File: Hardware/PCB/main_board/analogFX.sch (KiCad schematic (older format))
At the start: 40 parts, among them Q1 BC547, U1 MCP6002-xSN, U4 RC4558

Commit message: Add FX buffer and headphone amp to schematics
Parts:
- added C33: 100n, Capacitor_SMD:C_0805_2012Metric, symbol Device:C
- added R20: 3.9k, Resistor_SMD:R_0805_2012Metric, symbol Device:R
- added R21: 10k, Resistor_SMD:R_0805_2012Metric, symbol Device:R
- Q1: value BC547 -> BC547B
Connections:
- net labels added: 2.5V_midpoint, IN_DIST, OUT_VCF
- net labels removed: OUT_VCF__IN_DIST
- wire segments 123 -> 127
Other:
- note added: "buffer"
- moved on the sheet: C1, R3, R5, R6, U1B
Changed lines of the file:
@@
-$EndComp
-$Comp
-L Amplifier_Operational:MCP6002-xSN U?
-U 2 1 5E64D29A
-P 6600 1950
-AR Path="/5E64D29A" Ref="U?"  Part="2"
-AR Path="/5E632F77/5E64D29A" Ref="U1"  Part="2"
-F 0 "U1" H 6600 2317 50  0000 C CNN
-F 1 "MCP6002-xSN" H 6600 2226 50  0000 C CNN
-F 2 "Package_SO:SOIC-8_3.9x4.9mm_P1.27mm" H 6600 1950 50  0001 C CNN
-F 3 "http://ww1.microchip.com/downloads/en/DeviceDoc/21733j.pdf" H 6600 1950 50  0001 C CNN
-	2    6600 1950
-	1    0    0    -1
 $EndComp
 $Comp
 L Device:R R?
 U 1 1 5E64D2A0
-P 3200 2800
+P 2850 2800
 AR Path="/5E64D2A0" Ref="R?"  Part="1"
 AR Path="/5E632F77/5E64D2A0" Ref="R6"  Part="1"
-F 0 "R6" H 3270 2846 50  0000 L CNN
-F 1 "100k" H 3270 2755 50  0000 L CNN
-F 2 "Resistor_SMD:R_0805_2012Metric" V 3130 2800 50  0001 C CNN
-F 3 "~" H 3200 2800 50  0001 C CNN
-	1    3200 2800
+F 0 "R6" H 2920 2846 50  0000 L CNN
+F 1 "100k" H 2920 2755 50  0000 L CNN
+F 2 "Resistor_SMD:R_0805_2012Metric" V 2780 2800 50  0001 C CNN
+F 3 "~" H 2850 2800 50  0001 C CNN
+	1    2850 2800
 	1    0    0    -1
 $EndComp
@@
 L power:+5VA #PWR?
 U 1 1 5E64D2A6
-P 2750 2550
+P 2400 2550
 AR Path="/5E64D2A6" Ref="#PWR?"  Part="1"
 AR Path="/5E632F77/5E64D2A6" Ref="#PWR04"  Part="1"
-F 0 "#PWR04" H 2750 2400 50  0001 C CNN
-F 1 "+5VA" V 2765 2677 50  0000 L CNN
-F 2 "" H 2750 2550 50  0001 C CNN
-F 3 "" H 2750 2550 50  0001 C CNN
-	1    2750 2550
+F 0 "#PWR04" H 2400 2400 50  0001 C CNN
+F 1 "+5VA" V 2415 2677 50  0000 L CNN
+F 2 "" H 2400 2550 50  0001 C CNN
+F 3 "" H 2400 2550 50  0001 C CNN
+	1    2400 2550
 	0    -1   -1   0
 $EndComp
@@
 L power:GND #PWR?
 U 1 1 5E64D2AC
-P 3200 3000
+P 2850 3000
 AR Path="/5E64D2AC" Ref="#PWR?"  Part="1"
 AR Path="/5E632F77/5E64D2AC" Ref="#PWR06"  Part="1"
-F 0 "#PWR06" H 3200 2750 50  0001 C CNN
-F 1 "GND" H 3205 2827 50  0000 C CNN
-F 2 "" H 3200 3000 50  0001 C CNN
-F 3 "" H 3200 3000 50  0001 C CNN
-	1    3200 3000
+F 0 "#PWR06" H 2850 2750 50  0001 C CNN
+F 1 "GND" H 2855 2827 50  0000 C CNN
+F 2 "" H 2850 3000 50  0001 C CNN
+F 3 "" H 2850 3000 50  0001 C CNN
+	1    2850 3000
 	1    0    0    -1
 $EndComp
@@
 L Device:R R?
 U 1 1 5E64D2B8
-P 2950 2550
+P 2600 2550
 AR Path="/5E64D2B8" Ref="R?"  Part="1"
 AR Path="/5E632F77/5E64D2B8" Ref="R5"  Part="1"
-F 0 "R5" V 3050 2550 50  0000 C CNN
-F 1 "100k" V 3150 2550 50  0000 C CNN
-F 2 "Resistor_SMD:R_0805_2012Metric" V 2880 2550 50  0001 C CNN
-F 3 "~" H 2950 2550 50  0001 C CNN
-	1    2950 2550
+F 0 "R5" V 2700 2550 50  0000 C CNN
+F 1 "100k" V 2800 2550 50  0000 C CNN
+F 2 "Resistor_SMD:R_0805_2012Metric" V 2530 2550 50  0001 C CNN
+F 3 "~" H 2600 2550 50  0001 C CNN
+	1    2600 2550
 	0    1    1    0
 $EndComp
@@
 L Device:R R?
 U 1 1 5E64D2BE
-P 2150 2550
+P 1750 2550
 AR Path="/5E64D2BE" Ref="R?"  Part="1"
 AR Path="/5E632F77/5E64D2BE" Ref="R3"  Part="1"
-F 0 "R3" H 2080 2504 50  0000 R CNN
-F 1 "100k" H 2080 2595 50  0000 R CNN
-F 2 "Resistor_SMD:R_0805_2012Metric" V 2080 2550 50  0001 C CNN
-F 3 "~" H 2150 2550 50  0001 C CNN
-	1    2150 2550
+F 0 "R3" H 1680 2504 50  0000 R CNN
+F 1 "100k" H 1680 2595 50  0000 R CNN
+F 2 "Resistor_SMD:R_0805_2012Metric" V 1680 2550 50  0001 C CNN
+F 3 "~" H 1750 2550 50  0001 C CNN
+	1    1750 2550
 	-1   0    0    1
 $EndComp
@@
 L power:GND #PWR?
 U 1 1 5E64D2C4
-P 2150 2750
+P 1750 2750
 AR Path="/5E64D2C4" Ref="#PWR?"  Part="1"
 AR Path="/5E632F77/5E64D2C4" Ref="#PWR03"  Part="1"
-F 0 "#PWR03" H 2150 2500 50  0001 C CNN
-F 1 "GND" H 2155 2577 50  0000 C CNN
-F 2 "" H 2150 2750 50  0001 C CNN
-F 3 "" H 2150 2750 50  0001 C CNN
-	1    2150 2750
+F 0 "#PWR03" H 1750 2500 50  0001 C CNN
+F 1 "GND" H 1755 2577 50  0000 C CNN
+F 2 "" H 1750 2750 50  0001 C CNN
+F 3 "" H 1750 2750 50  0001 C CNN
+	1    1750 2750
 	1    0    0    -1
 $EndComp
@@
 AR Path="/5E632F77/5E64D2DC" Ref="Q1"  Part="1"
 F 0 "Q1" H 3041 1496 50  0000 L CNN
-F 1 "BC547" H 3041 1405 50  0000 L CNN
+F 1 "BC547B" H 3041 1405 50  0000 L CNN
 F 2 "Package_TO_SOT_THT:TO-92_Inline" H 3050 1375 50  0001 L CIN
 F 3 "http://www.fairchildsemi.com/ds/BC/BC547.pdf" H 2850 1450 50  0001 L CNN
@@
 L Device:C C?
 U 1 1 5E64D2FA
-P 1900 2350
+P 1500 2350
 AR Path="/5E64D2FA" Ref="C?"  Part="1"
 AR Path="/5E632F77/5E64D2FA" Ref="C1"  Part="1"
-F 0 "C1" V 1648 2350 50  0000 C CNN
-F 1 "4.7u" V 1739 2350 50  0000 C CNN
-F 2 "Capacitor_SMD:C_0805_2012Metric" H 1938 2200 50  0001 C CNN
-F 3 "~" H 1900 2350 50  0001 C CNN
-	1    1900 2350
+F 0 "C1" V 1248 2350 50  0000 C CNN
+F 1 "4.7u" V 1339 2350 50  0000 C CNN
+F 2 "Capacitor_SMD:C_0805_2012Metric" H 1538 2200 50  0001 C CNN
+F 3 "~" H 1500 2350 50  0001 C CNN
+	1    1500 2350
 	0    1    1    0
 $EndComp
@@
 $EndComp
 Wire Wire Line
-	2050 2350 2150 2350
-Wire Wire Line
-	2150 2400 2150 2350
-Connection ~ 2150 2350
-Wire Wire Line
-	2150 2350 2800 2350
-Wire Wire Line
-	2150 2750 2150 2700
-Wire Wire Line
-	2800 2550 2750 2550
+	1650 2350 1750 2350
+Wire Wire Line
+	1750 2400 1750 2350
+Connection ~ 1750 2350
+Wire Wire Line
+	1750 2350 2800 2350
+Wire Wire Line
+	1750 2750 1750 2700
+Wire Wire Line
+	2450 2550 2400 2550
 Wire Wire Line
 	3100 2350 3200 2350
 Wire Wire Line
-	3100 2550 3200 2550
-Wire Wire Line
-	3200 2650 3200 2550
-Connection ~ 3200 2550
-Wire Wire Line
-	3200 2550 3300 2550
+	2750 2550 2850 2550
+Wire Wire Line
+	2850 2650 2850 2550
+Connection ~ 2850 2550
+Wire Wire Line
+	2850 2550 3300 2550
 Wire Wire Line
 	1550 1650 1550 1600
@@
 	1950 950  1200 950
 Wire Wire Line
-	1750 2350 1200 2350
+	1350 2350 1200 2350
 Wire Wire Line
 	2250 1450 2500 1450
@@
 Connection ~ 4600 1250
 Wire Wire Line
-	3200 2950 3200 3000
+	2850 2950 2850 3000
 Wire Notes Line
 	700  700  5300 700
@@
 Text HLabel 1200 2350 0    50   Input ~ 0
 AUDIO_IN
-Wire Wire Line
-	6300 2050 6200 2050
-Wire Wire Line
-	6200 2050 6200 2300
-Wire Wire Line
-	6200 2300 7050 2300
-Wire Wire Line
-	7050 2300 7050 1950
-Wire Wire Line
-	7050 1950 6900 1950
-$Comp
-L power:GND #PWR0101
-U 1 1 5E6BBB3D
-P 6000 1900
-F 0 "#PWR0101" H 6000 1650 50  0001 C CNN
-F 1 "GND" H 6005 1727 50  0000 C CNN
-F 2 "" H 6000 1900 50  0001 C CNN
-F 3 "" H 6000 1900 50  0001 C CNN
-	1    6000 1900
-	1    0    0    -1
-$EndComp
-Wire Wire Line
-	6000 1900 6000 1850
-Wire Wire Line
-	6000 1850 6300 1850
 $Comp
 L Device:R_POT RV?
@@
 Connection ~ 3050 5150
 Text Label 1400 5950 2    50   ~ 0
-OUT_VCF__IN_DIST
+IN_DIST
 Text Label 4550 2450 0    50   ~ 0
-OUT_VCF__IN_DIST
+OUT_VCF
 Wire Wire Line
 	4300 2450 4550 2450
@@
 NoConn ~ 10300 4750
 NoConn ~ 10300 4850
+$Comp
+L Device:C C?
+U 1 1 5E791194
+P 7600 2100
+AR Path="/5E791194" Ref="C?"  Part="1"
+AR Path="/5E632F77/5E791194" Ref="C33"  Part="1"
+F 0 "C33" V 7348 2100 50  0000 C CNN
+F 1 "100n" V 7439 2100 50  0000 C CNN
+F 2 "Capacitor_SMD:C_0805_2012Metric" H 7638 1950 50  0001 C CNN
+F 3 "~" H 7600 2100 50  0001 C CNN
+	1    7600 2100
+	0    1    1    0
+$EndComp
+Text Label 3250 2550 3    50   ~ 0
+2.5V_midpoint
+Wire Wire Line
+	7350 1600 7350 2100
+Wire Wire Line
+	7450 2100 7350 2100
+Wire Wire Line
+	7750 2100 7900 2100
+Text Label 7900 2100 0    50   ~ 0
+IN_DIST
+Wire Notes Line
+	5450 700  5450 3500
+Wire Notes Line
+	5450 3500 8600 3500
+Wire Notes Line
+	8600 3500 8600 700
+Wire Notes Line
+	8600 700  5450 700
+Text Notes 5500 3450 0    118  ~ 24
+buffer
+Connection ~ 7350 2100
+Text Label 5900 2000 2    50   ~ 0
+OUT_VCF
+Wire Wire Line
+	6200 2000 5900 2000
+Wire Wire Line
+	7350 2100 7250 2100
+Wire Wire Line
+	7000 1600 7350 1600
+Wire Wire Line
+	6600 2000 6650 2000
+Connection ~ 6600 2000
+Wire Wire Line
+	6600 1600 6600 2000
+Wire Wire Line
+	6700 1600 6600 1600
+Wire Wire Line
+	6500 2000 6600 2000
+$Comp
+L Device:R R?
+U 1 1 5E7E9D23
+P 6850 1600
+AR Path="/5E7E9D23" Ref="R?"  Part="1"
+AR Path="/5E632F77/5E7E9D23" Ref="R21"  Part="1"
+F 0 "R21" V 6643 1600 50  0000 C CNN
+F 1 "10k" V 6734 1600 50  0000 C CNN
+F 2 "Resistor_SMD:R_0805_2012Metric" V 6780 1600 50  0001 C CNN
+F 3 "~" H 6850 1600 50  0001 C CNN
+	1    6850 1600
+	0    1    1    0
+$EndComp
+$Comp
+L Device:R R?
+U 1 1 5E7E6E06
+P 6350 2000
+AR Path="/5E7E6E06" Ref="R?"  Part="1"
+AR Path="/5E632F77/5E7E6E06" Ref="R20"  Part="1"
+F 0 "R20" V 6143 2000 50  0000 C CNN
+F 1 "3.9k" V 6234 2000 50  0000 C CNN
+F 2 "Resistor_SMD:R_0805_2012Metric" V 6280 2000 50  0001 C CNN
+F 3 "~" H 6350 2000 50  0001 C CNN
+	1    6350 2000
+	0    1    1    0
+$EndComp
+Text Label 6400 2200 3    50   ~ 0
+2.5V_midpoint
+Wire Wire Line
+	6650 2200 6400 2200
+$Comp
+L Amplifier_Operational:MCP6002-xSN U?
+U 2 1 5E64D29A
+P 6950 2100
+AR Path="/5E64D29A" Ref="U?"  Part="2"
+AR Path="/5E632F77/5E64D29A" Ref="U1"  Part="2"
+F 0 "U1" H 6950 2467 50  0000 C CNN
+F 1 "MCP6002-xSN" H 6950 2376 50  0000 C CNN
+F 2 "Package_SO:SOIC-8_3.9x4.9mm_P1.27mm" H 6950 2100 50  0001 C CNN
+F 3 "http://ww1.microchip.com/downloads/en/DeviceDoc/21733j.pdf" H 6950 2100 50  0001 C CNN
+	2    6950 2100
+	1    0    0    1
+$EndComp
 $EndSCHEMATC

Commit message: Route PCB changes
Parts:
- removed Q1: BC547B, Package_TO_SOT_THT:TO-92_Inline, symbol Transistor_BJT:BC547
- removed RV_VOL1: R_POT_Dual, Potentiometer_THT:Potentiometer_Alps_RK09L_Double_Vertical, symbol Device:R_POT_Dual
- added Q5: BC847B, Package_TO_SOT_SMD:SOT-23, symbol Transistor_BJT:BC847
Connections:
- no-connect marks 26 -> 20
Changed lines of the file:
@@
-$EndComp
-$Comp
-L Transistor_BJT:BC547 Q?
-U 1 1 5E64D2DC
-P 2850 1450
-AR Path="/5E64D2DC" Ref="Q?"  Part="1"
-AR Path="/5E632F77/5E64D2DC" Ref="Q1"  Part="1"
-F 0 "Q1" H 3041 1496 50  0000 L CNN
-F 1 "BC547B" H 3041 1405 50  0000 L CNN
-F 2 "Package_TO_SOT_THT:TO-92_Inline" H 3050 1375 50  0001 L CIN
-F 3 "http://www.fairchildsemi.com/ds/BC/BC547.pdf" H 2850 1450 50  0001 L CNN
-	1    2850 1450
-	1    0    0    -1
 $EndComp
 $Comp
@@
 Wire Wire Line
 	2250 950  2500 950
-Wire Wire Line
-	2500 950  2500 1450
 Connection ~ 2500 1450
 Wire Wire Line
@@
 $EndComp
 $Comp
-L Device:R_POT_Dual RV_VOL1
-U 1 1 5E599706
-P 9950 3350
-F 0 "RV_VOL1" H 9950 3117 50  0000 C CNN
-F 1 "R_POT_Dual" H 9950 3026 50  0000 C CNN
-F 2 "Potentiometer_THT:Potentiometer_Alps_RK09L_Double_Vertical" H 10200 3275 50  0001 C CNN
-F 3 "~" H 10200 3275 50  0001 C CNN
-	1    9950 3350
-	1    0    0    -1
-$EndComp
-$Comp
 L LED:HDSP-4840_2 BAR1
 U 1 1 5E5A0C61
@@
 Wire Notes Line
 	6800 3650 700  3650
-NoConn ~ 9550 3450
-NoConn ~ 9850 3450
-NoConn ~ 9700 3250
-NoConn ~ 10200 3250
-NoConn ~ 10050 3450
-NoConn ~ 10350 3450
 NoConn ~ 9900 4650
 NoConn ~ 9900 4750
@@
 	1    0    0    1
 $EndComp
+Wire Wire Line
+	2500 950  2500 1450
+$Comp
+L Transistor_BJT:BC847 Q5
+U 1 1 5EAE88EB
+P 2850 1450
+F 0 "Q5" H 3041 1496 50  0000 L CNN
+F 1 "BC847B" H 3041 1405 50  0000 L CNN
+F 2 "Package_TO_SOT_SMD:SOT-23" H 3050 1375 50  0001 L CIN
+F 3 "http://www.infineon.com/dgdl/Infineon-BC847SERIES_BC848SERIES_BC849SERIES_BC850SERIES-DS-v01_01-en.pdf?fileId=db3a304314dca389011541d4630a1657" H 2850 1450 50  0001 L CNN
+	1    2850 1450
+	1    0    0    -1
+$EndComp
 $EndSCHEMATC

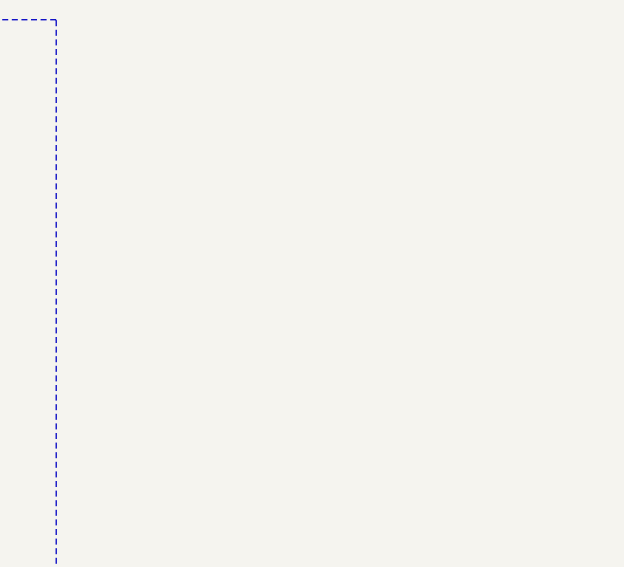
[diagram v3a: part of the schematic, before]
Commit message: Add test points headers
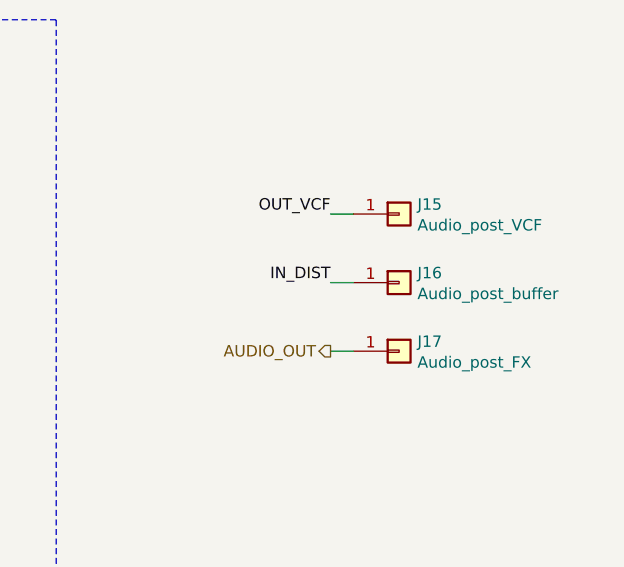
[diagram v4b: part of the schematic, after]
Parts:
- added J15: Audio_post_VCF, Connector_PinHeader_2.54mm:PinHeader_1x01_P2.54mm_Vertical, symbol Connector_Generic:Conn_01x01
- added J16: Audio_post_buffer, Connector_PinHeader_2.54mm:PinHeader_1x01_P2.54mm_Vertical, symbol Connector_Generic:Conn_01x01
- added J17: Audio_post_FX, Connector_PinHeader_2.54mm:PinHeader_1x01_P2.54mm_Vertical, symbol Connector_Generic:Conn_01x01
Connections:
- net AUDIO_OUT: now also J17.1 (Pin_1)
- net IN_DIST: now also J16.1 (Pin_1)
- net OUT_VCF: now also J15.1 (Pin_1)
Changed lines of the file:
@@
+	1    0    0    -1
+$EndComp
+Wire Wire Line
+	9900 2150 9800 2150
+Wire Wire Line
+	9900 1850 9800 1850
+Wire Wire Line
+	9900 1550 9800 1550
+Text Label 9800 1550 2    50   ~ 0
+OUT_VCF
+Text Label 9800 1850 2    50   ~ 0
+IN_DIST
+Text HLabel 9800 2150 0    50   Output ~ 0
+AUDIO_OUT
+$Comp
+L Connector_Generic:Conn_01x01 J?
+U 1 1 5E8DC2E2
+P 10100 1550
+AR Path="/5E57C92D/5E8DC2E2" Ref="J?"  Part="1"
+AR Path="/5E632F77/5E8DC2E2" Ref="J15"  Part="1"
+F 0 "J15" H 10180 1592 50  0000 L CNN
+F 1 "Audio_post_VCF" H 10180 1501 50  0000 L CNN
+F 2 "Connector_PinHeader_2.54mm:PinHeader_1x01_P2.54mm_Vertical" H 10100 1550 50  0001 C CNN
+F 3 "~" H 10100 1550 50  0001 C CNN
+	1    10100 1550
+	1    0    0    -1
+$EndComp
+$Comp
+L Connector_Generic:Conn_01x01 J?
+U 1 1 5E8E12D7
+P 10100 1850
+AR Path="/5E57C92D/5E8E12D7" Ref="J?"  Part="1"
+AR Path="/5E632F77/5E8E12D7" Ref="J16"  Part="1"
+F 0 "J16" H 10180 1892 50  0000 L CNN
+F 1 "Audio_post_buffer" H 10180 1801 50  0000 L CNN
+F 2 "Connector_PinHeader_2.54mm:PinHeader_1x01_P2.54mm_Vertical" H 10100 1850 50  0001 C CNN
+F 3 "~" H 10100 1850 50  0001 C CNN
+	1    10100 1850
+	1    0    0    -1
+$EndComp
+$Comp
+L Connector_Generic:Conn_01x01 J?
+U 1 1 5E8E1DAA
+P 10100 2150
+AR Path="/5E57C92D/5E8E1DAA" Ref="J?"  Part="1"
+AR Path="/5E632F77/5E8E1DAA" Ref="J17"  Part="1"
+F 0 "J17" H 10180 2192 50  0000 L CNN
+F 1 "Audio_post_FX" H 10180 2101 50  0000 L CNN
+F 2 "Connector_PinHeader_2.54mm:PinHeader_1x01_P2.54mm_Vertical" H 10100 2150 50  0001 C CNN
+F 3 "~" H 10100 2150 50  0001 C CNN
+	1    10100 2150
 	1    0    0    -1
 $EndComp

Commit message: Re-layout HMI, pre route
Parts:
- removed BAR1: HDSP-4840_2, Display:HDSP-4840, symbol LED:HDSP-4840_2
- J15: value Audio_post_VCF -> Post_VCF; footprint Connector_PinHeader_2.54mm:PinHeader_1x01_P2.54mm_Vertical -> TestPoint:TestPoint_THTPad_D1.0mm_Drill0.5mm; symbol Connector_Generic:Conn_01x01 -> Connector:TestPoint
- J16: value Audio_post_buffer -> Post_buffer; footprint Connector_PinHeader_2.54mm:PinHeader_1x01_P2.54mm_Vertical -> TestPoint:TestPoint_THTPad_D1.0mm_Drill0.5mm; symbol Connector_Generic:Conn_01x01 -> Connector:TestPoint
- J17: value Audio_post_FX -> Post_FX; footprint Connector_PinHeader_2.54mm:PinHeader_1x01_P2.54mm_Vertical -> TestPoint:TestPoint_THTPad_D1.0mm_Drill0.5mm; symbol Connector_Generic:Conn_01x01 -> Connector:TestPoint
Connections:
- no-connect marks 20 -> 0
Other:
- note added: "Test points"
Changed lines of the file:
@@
-$EndComp
-$Comp
-L LED:HDSP-4840_2 BAR1
-U 1 1 5E5A0C61
-P 10100 5050
-F 0 "BAR1" H 10100 5717 50  0000 C CNN
-F 1 "HDSP-4840_2" H 10100 5626 50  0000 C CNN
-F 2 "Display:HDSP-4840" H 10100 4250 50  0001 C CNN
-F 3 "https://docs.broadcom.com/docs/AV02-1798EN" H 8100 5250 50  0001 C CNN
-	1    10100 5050
-	1    0    0    -1
 $EndComp
 $Comp
@@
 Wire Notes Line
 	6800 3650 700  3650
-NoConn ~ 9900 4650
-NoConn ~ 9900 4750
-NoConn ~ 9900 4850
-NoConn ~ 9900 4950
-NoConn ~ 9900 5050
-NoConn ~ 9900 5150
-NoConn ~ 9900 5250
-NoConn ~ 9900 5350
-NoConn ~ 9900 5450
-NoConn ~ 9900 5550
-NoConn ~ 10300 5550
-NoConn ~ 10300 5450
-NoConn ~ 10300 5350
-NoConn ~ 10300 5250
-NoConn ~ 10300 5150
-NoConn ~ 10300 5050
-NoConn ~ 10300 4950
-NoConn ~ 10300 4650
-NoConn ~ 10300 4750
-NoConn ~ 10300 4850
 $Comp
 L Device:C C?
@@
 AUDIO_OUT
 $Comp
-L Connector_Generic:Conn_01x01 J?
+L Connector:TestPoint J?
 U 1 1 5E8DC2E2
-P 10100 1550
+P 9900 1550
 AR Path="/5E57C92D/5E8DC2E2" Ref="J?"  Part="1"
 AR Path="/5E632F77/5E8DC2E2" Ref="J15"  Part="1"
-F 0 "J15" H 10180 1592 50  0000 L CNN
-F 1 "Audio_post_VCF" H 10180 1501 50  0000 L CNN
-F 2 "Connector_PinHeader_2.54mm:PinHeader_1x01_P2.54mm_Vertical" H 10100 1550 50  0001 C CNN
-F 3 "~" H 10100 1550 50  0001 C CNN
-	1    10100 1550
-	1    0    0    -1
-$EndComp
-$Comp
-L Connector_Generic:Conn_01x01 J?
+F 0 "J15" V 9980 1592 50  0000 L CNN
+F 1 "Post_VCF" V 9900 1750 50  0000 L CNN
+F 2 "TestPoint:TestPoint_THTPad_D1.0mm_Drill0.5mm" H 9900 1550 50  0001 C CNN
+F 3 "~" H 9900 1550 50  0001 C CNN
+	1    9900 1550
+	0    1    1    0
+$EndComp
+$Comp
+L Connector:TestPoint J?
 U 1 1 5E8E12D7
-P 10100 1850
+P 9900 1850
 AR Path="/5E57C92D/5E8E12D7" Ref="J?"  Part="1"
 AR Path="/5E632F77/5E8E12D7" Ref="J16"  Part="1"
-F 0 "J16" H 10180 1892 50  0000 L CNN
-F 1 "Audio_post_buffer" H 10180 1801 50  0000 L CNN
-F 2 "Connector_PinHeader_2.54mm:PinHeader_1x01_P2.54mm_Vertical" H 10100 1850 50  0001 C CNN
-F 3 "~" H 10100 1850 50  0001 C CNN
-	1    10100 1850
-	1    0    0    -1
-$EndComp
-$Comp
-L Connector_Generic:Conn_01x01 J?
+F 0 "J16" V 9980 1892 50  0000 L CNN
+F 1 "Post_buffer" V 9900 2050 50  0000 L CNN
+F 2 "TestPoint:TestPoint_THTPad_D1.0mm_Drill0.5mm" H 9900 1850 50  0001 C CNN
+F 3 "~" H 9900 1850 50  0001 C CNN
+	1    9900 1850
+	0    1    1    0
+$EndComp
+$Comp
+L Connector:TestPoint J?
 U 1 1 5E8E1DAA
-P 10100 2150
+P 9900 2150
 AR Path="/5E57C92D/5E8E1DAA" Ref="J?"  Part="1"
 AR Path="/5E632F77/5E8E1DAA" Ref="J17"  Part="1"
-F 0 "J17" H 10180 2192 50  0000 L CNN
-F 1 "Audio_post_FX" H 10180 2101 50  0000 L CNN
-F 2 "Connector_PinHeader_2.54mm:PinHeader_1x01_P2.54mm_Vertical" H 10100 2150 50  0001 C CNN
-F 3 "~" H 10100 2150 50  0001 C CNN
-	1    10100 2150
-	1    0    0    -1
-$EndComp
+F 0 "J17" V 9980 2192 50  0000 L CNN
+F 1 "Post_FX" V 9900 2350 50  0000 L CNN
+F 2 "TestPoint:TestPoint_THTPad_D1.0mm_Drill0.5mm" H 9900 2150 50  0001 C CNN
+F 3 "~" H 9900 2150 50  0001 C CNN
+	1    9900 2150
+	0    1    1    0
+$EndComp
+Text Notes 9600 2450 0    118  ~ 0
+Test points
 $EndSCHEMATC

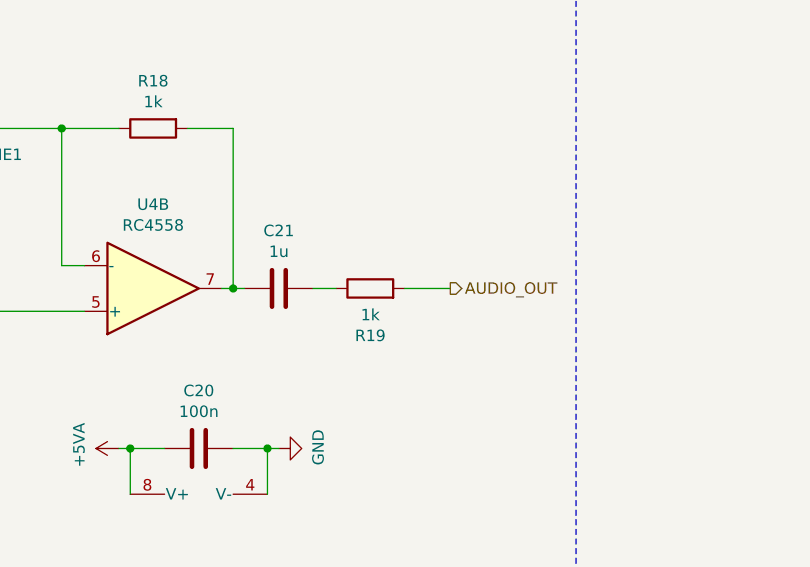
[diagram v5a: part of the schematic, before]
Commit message: Use headphone amp IC instead of discrete amp
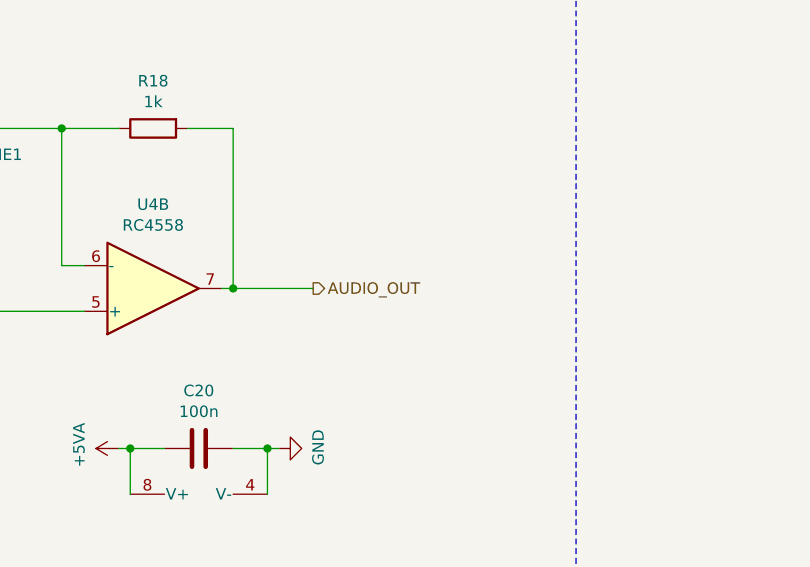
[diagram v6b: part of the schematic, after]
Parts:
- removed C21: 1u, Capacitor_SMD:C_0805_2012Metric, symbol Device:C
- removed R19: 1k, Resistor_SMD:R_0805_2012Metric, symbol Device:R
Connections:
- net AUDIO_OUT: now also R18.2, U4.7
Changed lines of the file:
@@
 Wire Wire Line
 	5000 3150 5050 3150
-Text HLabel 6250 5500 2    50   Output ~ 0
+Text HLabel 5650 5500 2    50   Output ~ 0
 AUDIO_OUT
 Text HLabel 1200 950  0    50   Input ~ 0
@@
 	0    -1   1    0
 $EndComp
-$Comp
-L Device:C C?
-U 1 1 5E765B1E
-P 5500 5500
-AR Path="/5E765B1E" Ref="C?"  Part="1"
-AR Path="/5E632F77/5E765B1E" Ref="C21"  Part="1"
-F 0 "C21" V 5248 5500 50  0000 C CNN
-F 1 "1u" V 5339 5500 50  0000 C CNN
-F 2 "Capacitor_SMD:C_0805_2012Metric" H 5538 5350 50  0001 C CNN
-F 3 "~" H 5500 5500 50  0001 C CNN
-	1    5500 5500
-	0    1    1    0
-$EndComp
-$Comp
-L Device:R R?
-U 1 1 5E7661F5
-P 5900 5500
-AR Path="/5E7661F5" Ref="R?"  Part="1"
-AR Path="/5E632F77/5E7661F5" Ref="R19"  Part="1"
-F 0 "R19" V 5693 5500 50  0000 C CNN
-F 1 "1k" V 5784 5500 50  0000 C CNN
-F 2 "Resistor_SMD:R_0805_2012Metric" V 5830 5500 50  0001 C CNN
-F 3 "~" H 5900 5500 50  0001 C CNN
-	1    5900 5500
-	0    -1   -1   0
-$EndComp
 Wire Wire Line
 	3350 4300 3350 4250
@@
 Wire Wire Line
 	5300 5500 5250 5500
-Wire Wire Line
-	5300 5500 5350 5500
 Connection ~ 5300 5500
-Wire Wire Line
-	5650 5500 5750 5500
-Wire Wire Line
-	6050 5500 6250 5500
 $Comp
 L Device:C C?
@@
 Text Notes 9600 2450 0    118  ~ 0
 Test points
+Wire Wire Line
+	5300 5500 5650 5500
 $EndSCHEMATC
